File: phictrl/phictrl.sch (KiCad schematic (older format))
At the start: 5 parts, among them J1 Conn_01x04_Female

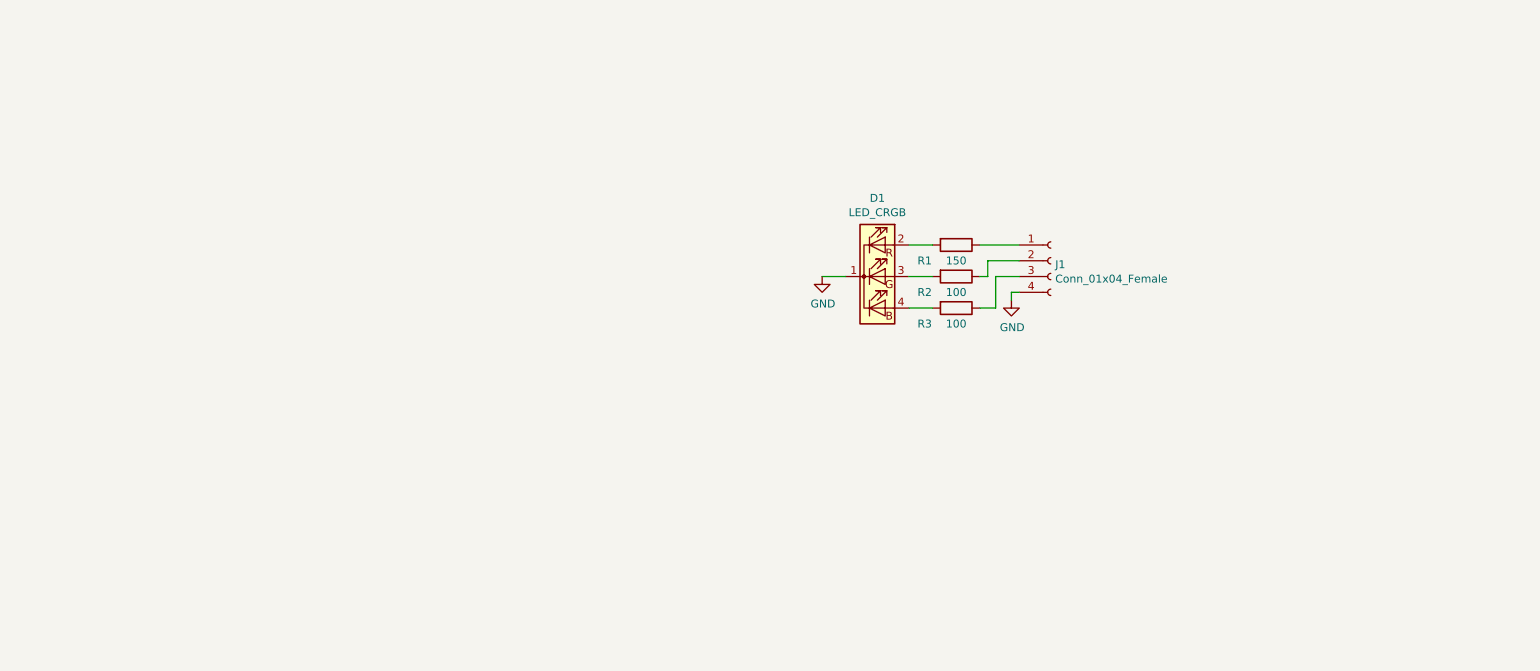
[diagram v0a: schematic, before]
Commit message: Planned pins and developed LED PCB.
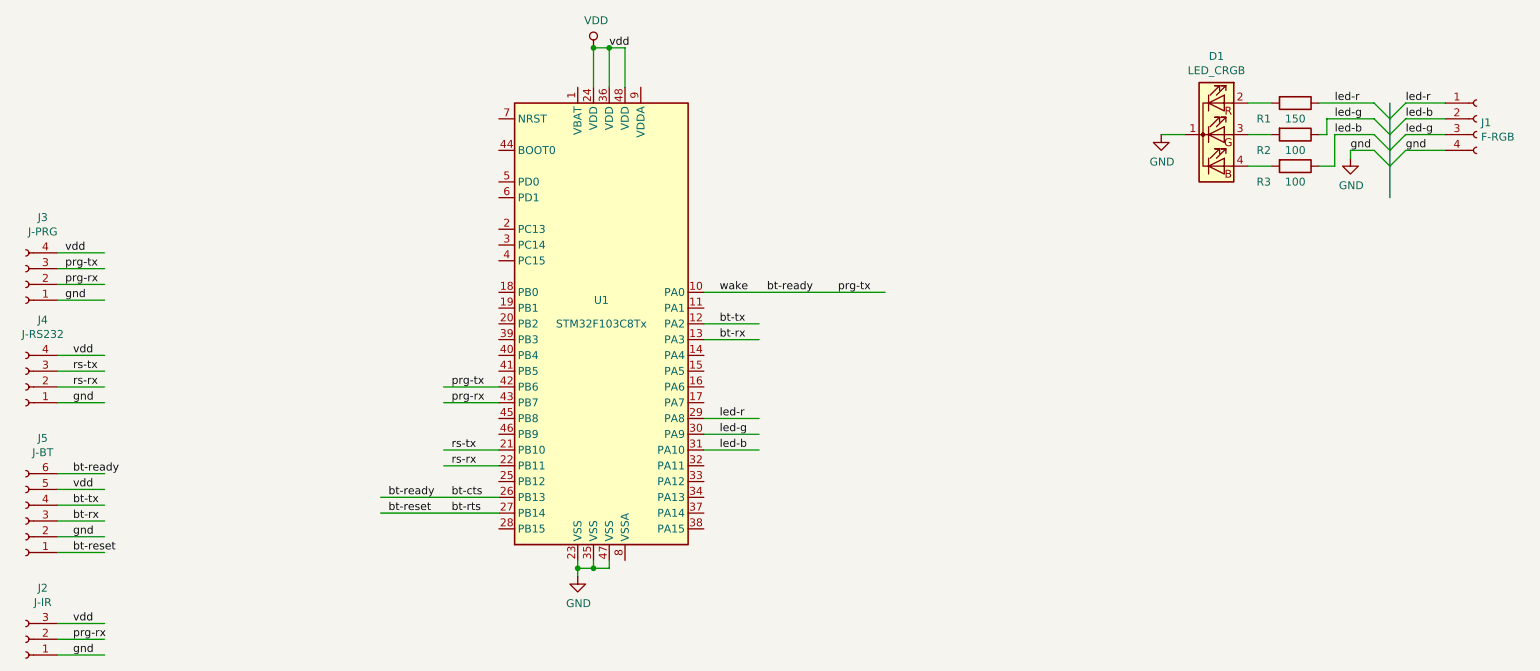
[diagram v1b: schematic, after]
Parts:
- added J2: J-IR, Connector_PinHeader_2.54mm:PinHeader_1x03_P2.54mm_Vertical, symbol Connector:Conn_01x03_Female
- added J3: J-PRG, Connector_PinHeader_2.54mm:PinHeader_1x04_P2.54mm_Vertical, symbol Connector:Conn_01x04_Female
- added J4: J-RS232, Connector_PinHeader_2.54mm:PinHeader_1x04_P2.54mm_Vertical, symbol Connector:Conn_01x04_Female
- added J5: J-BT, Connector_PinHeader_2.54mm:PinHeader_1x06_P2.54mm_Vertical, symbol Connector:Conn_01x06_Female
- added U1: STM32F103C8Tx, Package_QFP:LQFP-48_7x7mm_P0.5mm, symbol MCU_ST_STM32F1:STM32F103C8Tx
- D1: footprint (none) -> LED_THT:LED_D5.0mm-4_RGB
- J1: value Conn_01x04_Female -> F-RGB; footprint (none) -> Connector_Wire:SolderWirePad_1x04_P3.81mm_Drill1mm
- R1, R2, R3: footprint (none) -> Resistor_SMD:R_0805_2012Metric_Pad1.15x1.40mm_HandSolder
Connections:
- net labels added: VDD, bt-cts, bt-ready, bt-reset, bt-rts, bt-rx, bt-tx, gnd, led-b, led-g, led-r, prg-rx, prg-tx, rs-rx, rs-tx, vdd, wake
- wire segments 13 -> 57
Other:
- moved on the sheet: D1, J1, R1, R2, R3

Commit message: Printed PCB
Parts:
- removed D1: LED_CRGB, LED_THT:LED_D5.0mm-4_RGB, symbol Device:LED_CRGB
- added D1: LED_RCBG, LED_THT:LED_D5.0mm-4_RGB, symbol Device:LED_RCBG
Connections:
- net labels added: B, G, R
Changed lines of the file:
@@
 $EndDescr
-$Comp
-L Device:LED_CRGB D1
-U 1 1 5E3BE33A
-P 9000 1250
-F 0 "D1" H 9000 1747 50  0000 C CNN
-F 1 "LED_CRGB" H 9000 1656 50  0000 C CNN
-F 2 "LED_THT:LED_D5.0mm-4_RGB" H 9000 1200 50  0001 C CNN
-F 3 "~" H 9000 1200 50  0001 C CNN
-	1    9000 1250
-	1    0    0    -1
-$EndComp
 $Comp
 L Device:R R1
@@
 Wire Bus Line
 	10100 1050 10100 1650
+$Comp
+L Device:LED_RCBG D1
+U 1 1 5E3D3ECB
+P 9000 1250
+F 0 "D1" H 9000 1747 50  0000 C CNN
+F 1 "LED_RCBG" H 9000 1656 50  0000 C CNN
+F 2 "LED_THT:LED_D5.0mm-4_RGB" H 9000 1200 50  0001 C CNN
+F 3 "~" H 9000 1200 50  0001 C CNN
+	1    9000 1250
+	1    0    0    -1
+$EndComp
+Text Label 9250 1450 0    50   ~ 0
+G
+Text Label 9250 1250 0    50   ~ 0
+B
+Text Label 9250 1050 0    50   ~ 0
+R
 $EndSCHEMATC
